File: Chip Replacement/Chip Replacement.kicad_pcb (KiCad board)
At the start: 2 copper layers, 13 x 11.5 mm, 2 parts, among them J2 Conn_01x14_Socket, U1 BGA153 UFS Modified

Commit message: V1.1
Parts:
- moved J2 0.90 mm to (150.0, 99.1), turned to 180 degrees
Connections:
- J2 pad 1: VCC -> /TX1P
- J2 pad 10: /TX0N -> /RX1P
- J2 pad 11: /TX0P -> VCC
- J2 pad 12: /TX1N -> VCCQ2
- J2 pad 13: /TX1P -> VCCQ
- J2 pad 2: VCCQ -> /TX1N
- J2 pad 3: VCCQ2 -> /TX0P
- J2 pad 4: /RX1P -> /TX0N
- J2 pad 5: /RX1N -> /REF_CLK
- J2 pad 6: /RX0P -> /RST_N
- J2 pad 8: /RST_N -> /RX0P
- J2 pad 9: /REF_CLK -> /RX1N
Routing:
- net VCCQ: track 9.47 -> 20.0 mm
- net VCCQ2: track 9.53 -> 18.7 mm
- net /RX0P: track 1.75 -> 7.43 mm
- net /TX0N: track 1.75 -> 7.43 mm
- net /TX1N: track 1.75 -> 7.43 mm
- net /RX1P: track 1.75 -> 7.43 mm
- net /REF_CLK: track 2.70 -> 7.55 mm
- net /RST_N: track 1.75 -> 6.56 mm
- net /TX0P: track 2.70 -> 7.48 mm
- net /RX1N: track 2.70 -> 7.48 mm
- net /RX0N: track 2.70 -> 7.48 mm
- net /TX1P: track 2.70 -> 7.48 mm
- net VCC: track 12.8 -> 16.4 mm
- net VSS: track 29.7 -> 31.7 mm
- added copper zone on In1.Cu, net VSS
- added copper zone on In2.Cu, net VSS
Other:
- copper layers 2 -> 4

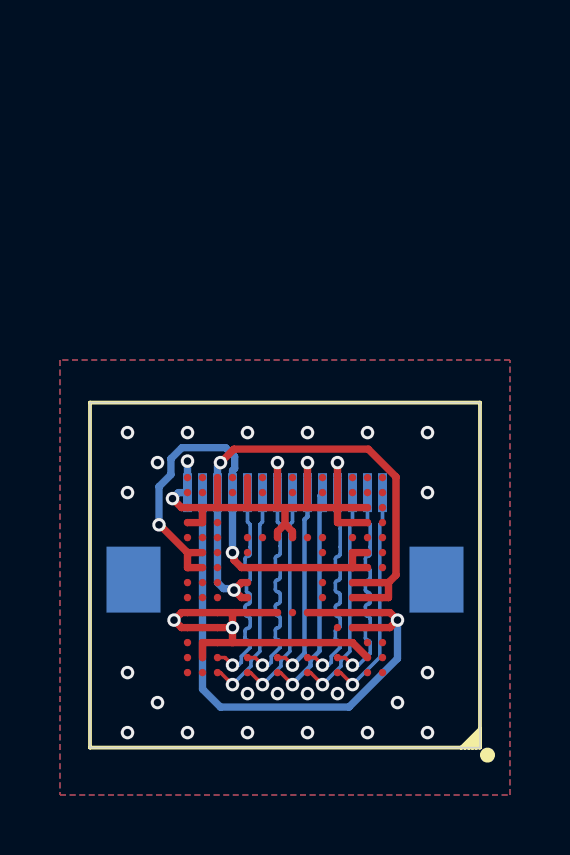
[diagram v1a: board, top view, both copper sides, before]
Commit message: V1.2 for forward fpc cable
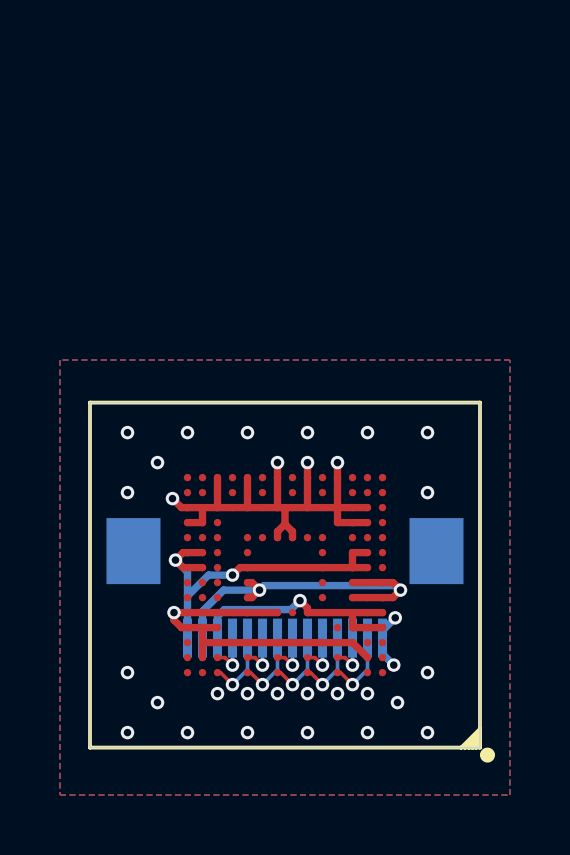
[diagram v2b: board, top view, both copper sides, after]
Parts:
- U1: value BGA153 UFS Modified -> BGA153 UFS Chip Replacement Modified
- moved J2 1.15 mm to (150.0, 100.2), turned to 0 degrees
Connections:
- J2 pad 1: /TX1P -> VCC
- J2 pad 10: /RX1P -> /TX0N
- J2 pad 11: VCC -> /TX0P
- J2 pad 12: VCCQ2 -> /TX1N
- J2 pad 13: VCCQ -> /TX1P
- J2 pad 2: /TX1N -> VCCQ2
- J2 pad 3: /TX0P -> VCCQ
- J2 pad 4: /TX0N -> /RX1P
- J2 pad 5: /REF_CLK -> /RX1N
- J2 pad 6: /RST_N -> /RX0P
- J2 pad 8: /RX0P -> /RST_N
- J2 pad 9: /RX1N -> /REF_CLK
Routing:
- net VCCQ: track 20.0 -> 8.20 mm
- net VCCQ2: track 18.7 -> 12.3 mm
- net /RX0P: track 7.43 -> 1.50 mm
- net /TX0N: track 7.43 -> 1.50 mm
- net /TX1N: track 7.43 -> 1.50 mm
- net /RX1P: track 7.43 -> 1.50 mm
- net /REF_CLK: track 7.55 -> 2.42 mm
- net /TX0P: track 7.48 -> 2.42 mm
- net /RX1N: track 7.48 -> 2.42 mm
- net /RX0N: track 7.48 -> 2.42 mm
- net /TX1P: track 7.48 -> 2.42 mm
- net /RST_N: track 6.56 -> 1.50 mm
- net VCC: track 16.4 -> 12.2 mm
- net VSS: track 31.7 -> 31.1 mm, vias 30 -> 32

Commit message: V1.3 GB042 Connector
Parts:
- removed J2: Conn_01x14_Socket, BGA153:FPC 14 Pin 0.5P
- added J1: GB042-30S-H10, BGA153:GB042-30S-H10, F.Cu at (150.0, 90.0)
- U1: moved to B.Cu
- moved U1 10.0 mm to (150.0, 90.0), turned to 180 degrees
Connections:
- U1 pad C1: unconnected-(U1-VDDiQ-PadC1) -> /VDDiQ
- U1 pad H1: unconnected-(U1-VDDiQ2-PadH1) -> /VDDiQ2
- U1 pad J1: unconnected-(U1-VDDi-PadJ1) -> /VDDi
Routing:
- net /RST_N: track 1.50 -> 17.4 mm
- net /VDDiQ: track 0.00 -> 9.48 mm, vias 0 -> 1
- net /VDDiQ2: track 0.00 -> 3.69 mm, vias 0 -> 1
- net VCCQ2: track 12.3 -> 8.67 mm
- net /VDDi: track 0.00 -> 2.59 mm, vias 0 -> 1
- net /TX1N: track 1.50 -> 2.70 mm
- net VSS: track 31.1 -> 30.0 mm, vias 32 -> 15
- net /TX0N: track 1.50 -> 2.62 mm
- net /RX0P: track 1.50 -> 2.62 mm
- net /RX1P: track 1.50 -> 2.54 mm
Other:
- outline, holes or cut-outs redrawn
